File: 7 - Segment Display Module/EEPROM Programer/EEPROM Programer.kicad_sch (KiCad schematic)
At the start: 3 parts, among them J1 Conn_01x02_Pin, U1 Pico, U3 AT28C64B-15PU

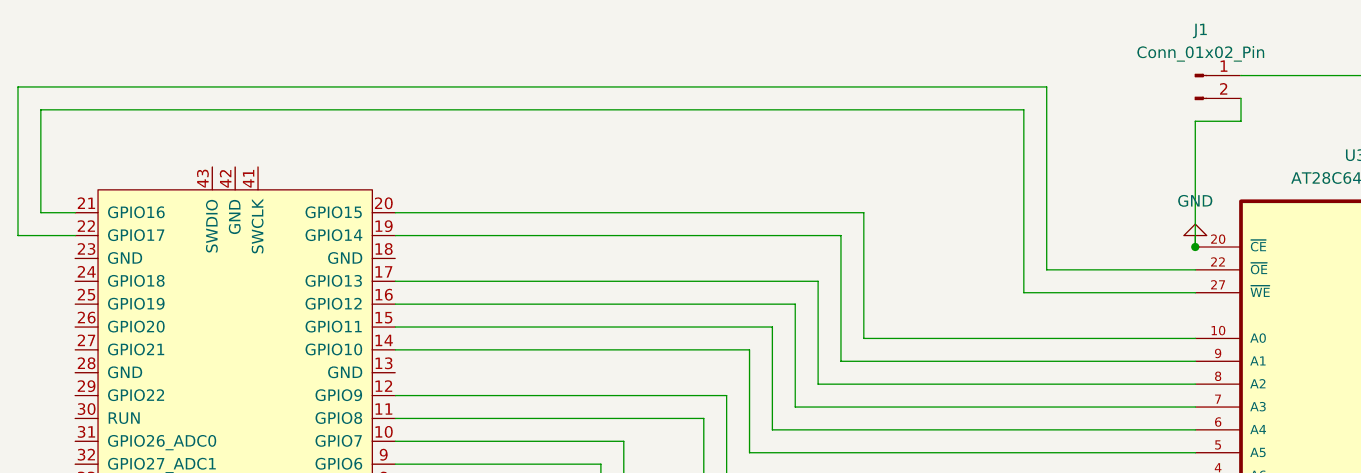
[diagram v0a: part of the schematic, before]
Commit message: Added a common ground with the pico and the EEPROM
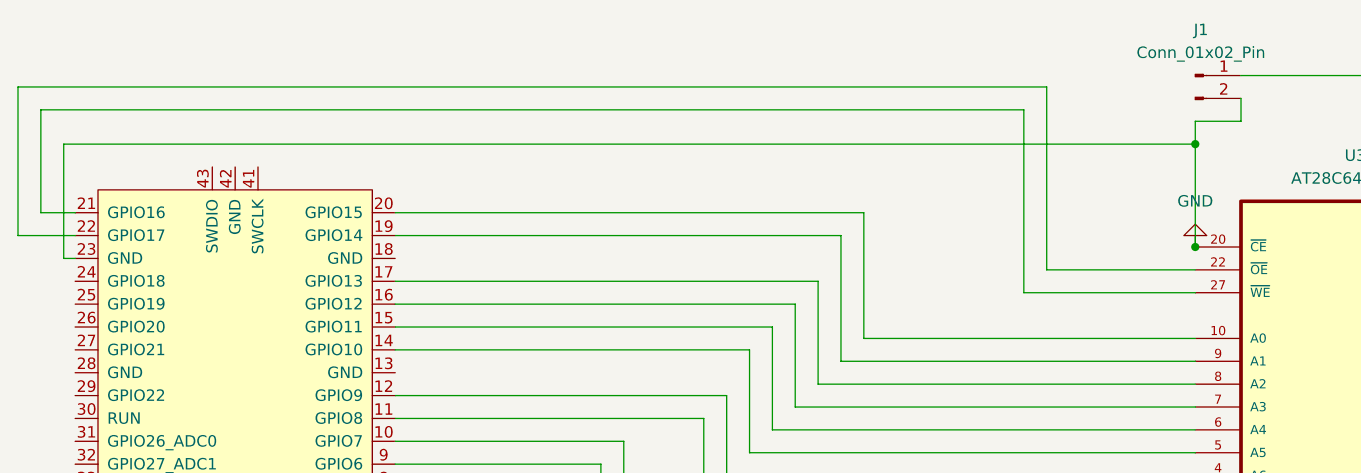
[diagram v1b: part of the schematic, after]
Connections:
- net GND: now also U1.23 (GND)
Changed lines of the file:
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@@
+	)
+	(junction
+		(at 149.86 44.45)
+		(diameter 0)
+		(color 0 0 0 0)
 	)
 	(junction
@@
 	(wire
 		(pts
-			(xy 149.86 55.88) (xy 149.86 41.91)
+			(xy 149.86 55.88) (xy 149.86 44.45)
 		)
 		(stroke
@@
 	(wire
 		(pts
+			(xy 149.86 44.45) (xy 24.13 44.45)
+		)
+		(stroke
+			(width 0)
+			(type default)
+		)
+	)
+	(wire
+		(pts
 			(xy 185.42 36.83) (xy 154.94 36.83)
 		)
@@
 	(wire
 		(pts
+			(xy 149.86 44.45) (xy 149.86 41.91)
+		)
+		(stroke
+			(width 0)
+			(type default)
+		)
+	)
+	(wire
+		(pts
 			(xy 133.35 38.1) (xy 19.05 38.1)
 		)
@@
 	(wire
 		(pts
+			(xy 24.13 57.15) (xy 25.4 57.15)
+		)
+		(stroke
+			(width 0)
+			(type default)
+		)
+	)
+	(wire
+		(pts
 			(xy 149.86 71.12) (xy 107.95 71.12)
 		)
@@
 		)
 		(stroke
+			(width 0)
+			(type default)
+		)
+	)
+	(wire
+		(pts
+			(xy 24.13 44.45) (xy 24.13 57.15)
+		)
+		(stroke
